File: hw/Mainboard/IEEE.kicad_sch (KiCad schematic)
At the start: 25 parts, among them J3 IEEE, U2 SN74LS07, U3 SN74LS07, U4 SN74LS07, U5 74LS245, U6 74LS245

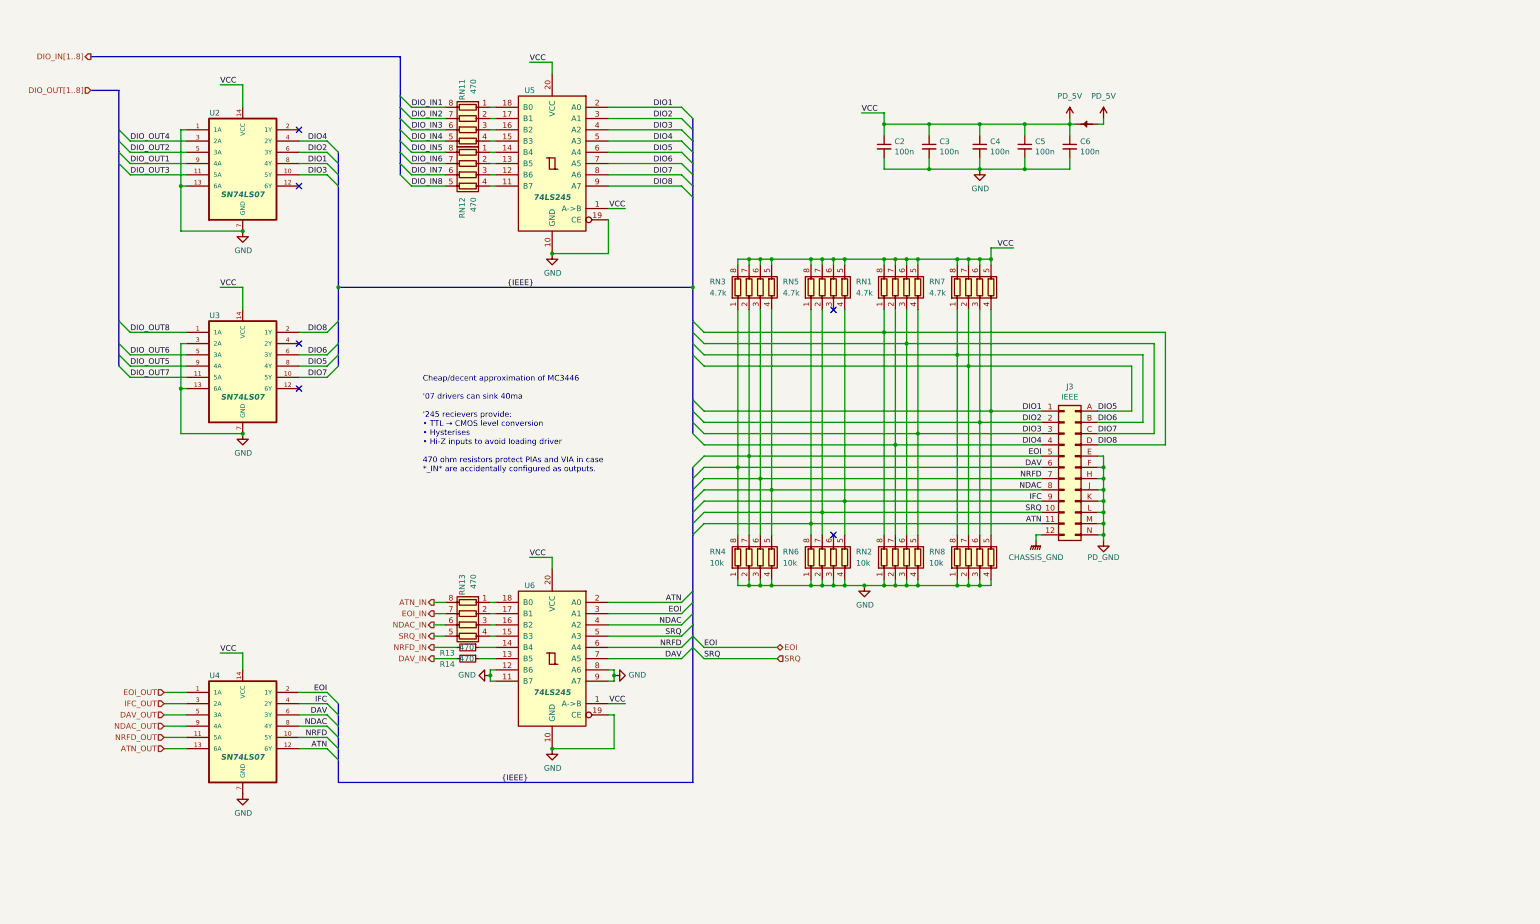
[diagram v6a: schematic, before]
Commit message: hw: tidy audio, cass, IEEE, keyboard, magic, user
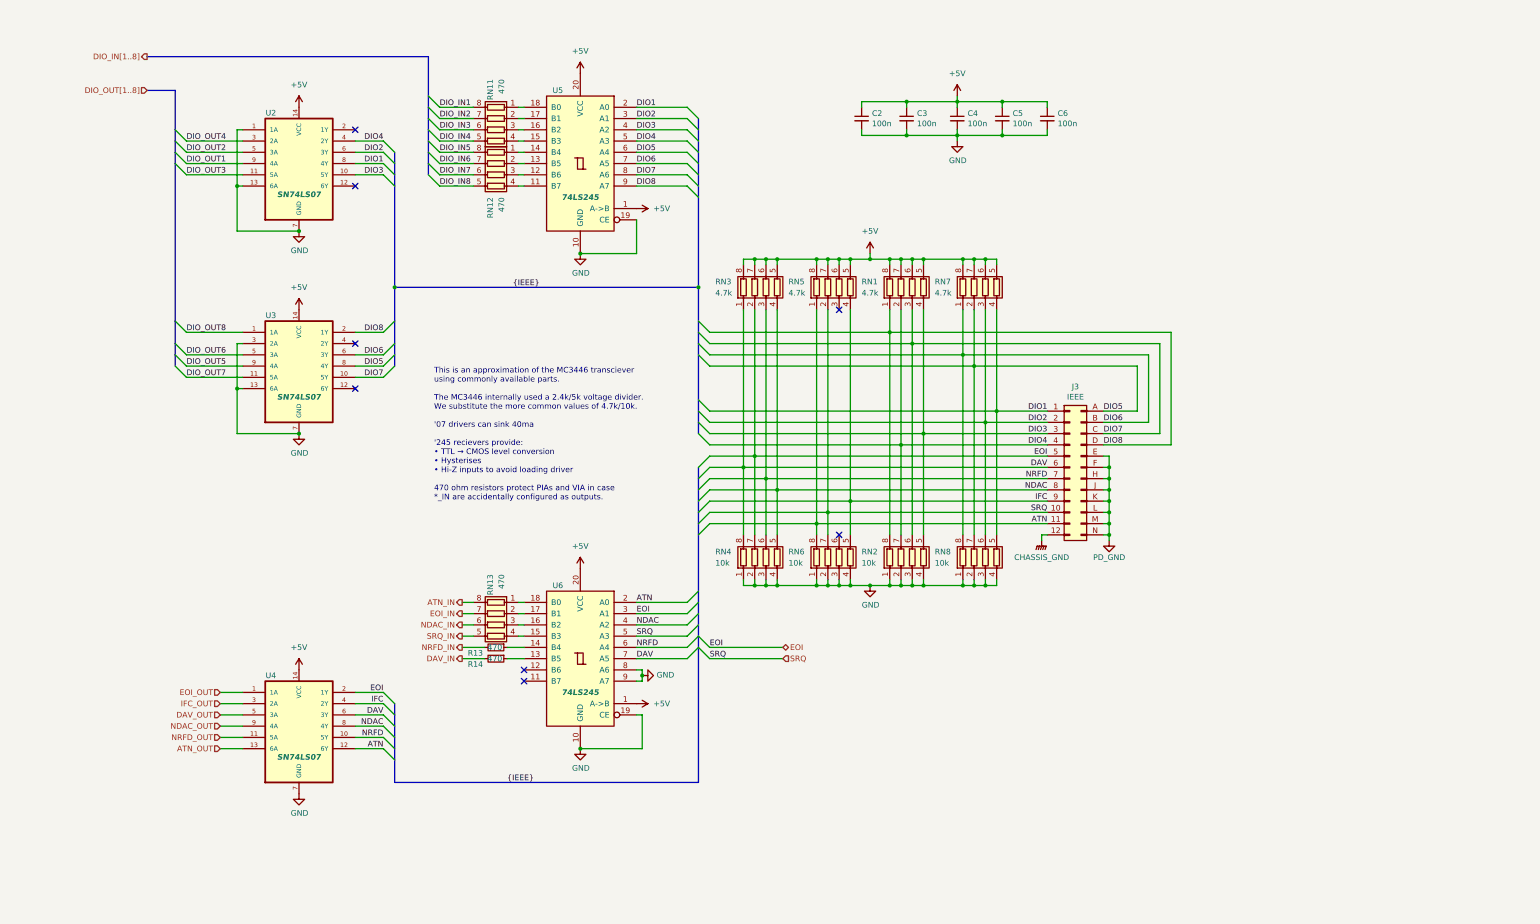
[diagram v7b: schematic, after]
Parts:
- removed PT5: PowerTie_2, PET:NetTie-2_SMD_Pad_1.6_to_0.4mm, symbol PET:PowerTie_2
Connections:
- net GND: no longer U6.11 (B7), U6.12 (B6)
- net PD_5V renamed +5V
- no-connect marks 6 -> 8
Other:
- note added: "This is an approximation of the MC3446 transciever using commonly available parts. The MC3446 internally used a 2.4k/5k voltage divider. We substitute the more common values of 4.7k/10k. '07 drivers can sink 40ma '245 recievers provide: • TTL → CMOS level conversion • Hysterises • Hi-Z inputs to avoid loading driver 470 ohm resistors protect PIAs and VIA in case *_IN are accidentally configured a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"
- note removed: "Cheap/decent approximation of MC3446 '07 drivers can sink 40ma '245 recievers provide: • TTL → CMOS level conversion • Hysterises • Hi-Z inputs to avoid loading driver 470 ohm resistors protect PIAs and VIA in case *_IN* are accidentally configured as outputs."
- moved on the sheet: C2, C3, C4, C5, C6, J3, R13, R14, RN1, RN11, RN12, RN13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
